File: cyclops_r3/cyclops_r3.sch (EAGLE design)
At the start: 102 parts, among them Q1 BC817, Q2 IRF510, U1 MCP4921, U2 MCP4022-50k, U3 317-N, U4 TLV3701, U5 337-N, U6 ADR03, U7 OP1177, U8 LTC2052HV, U9 ZXTD45

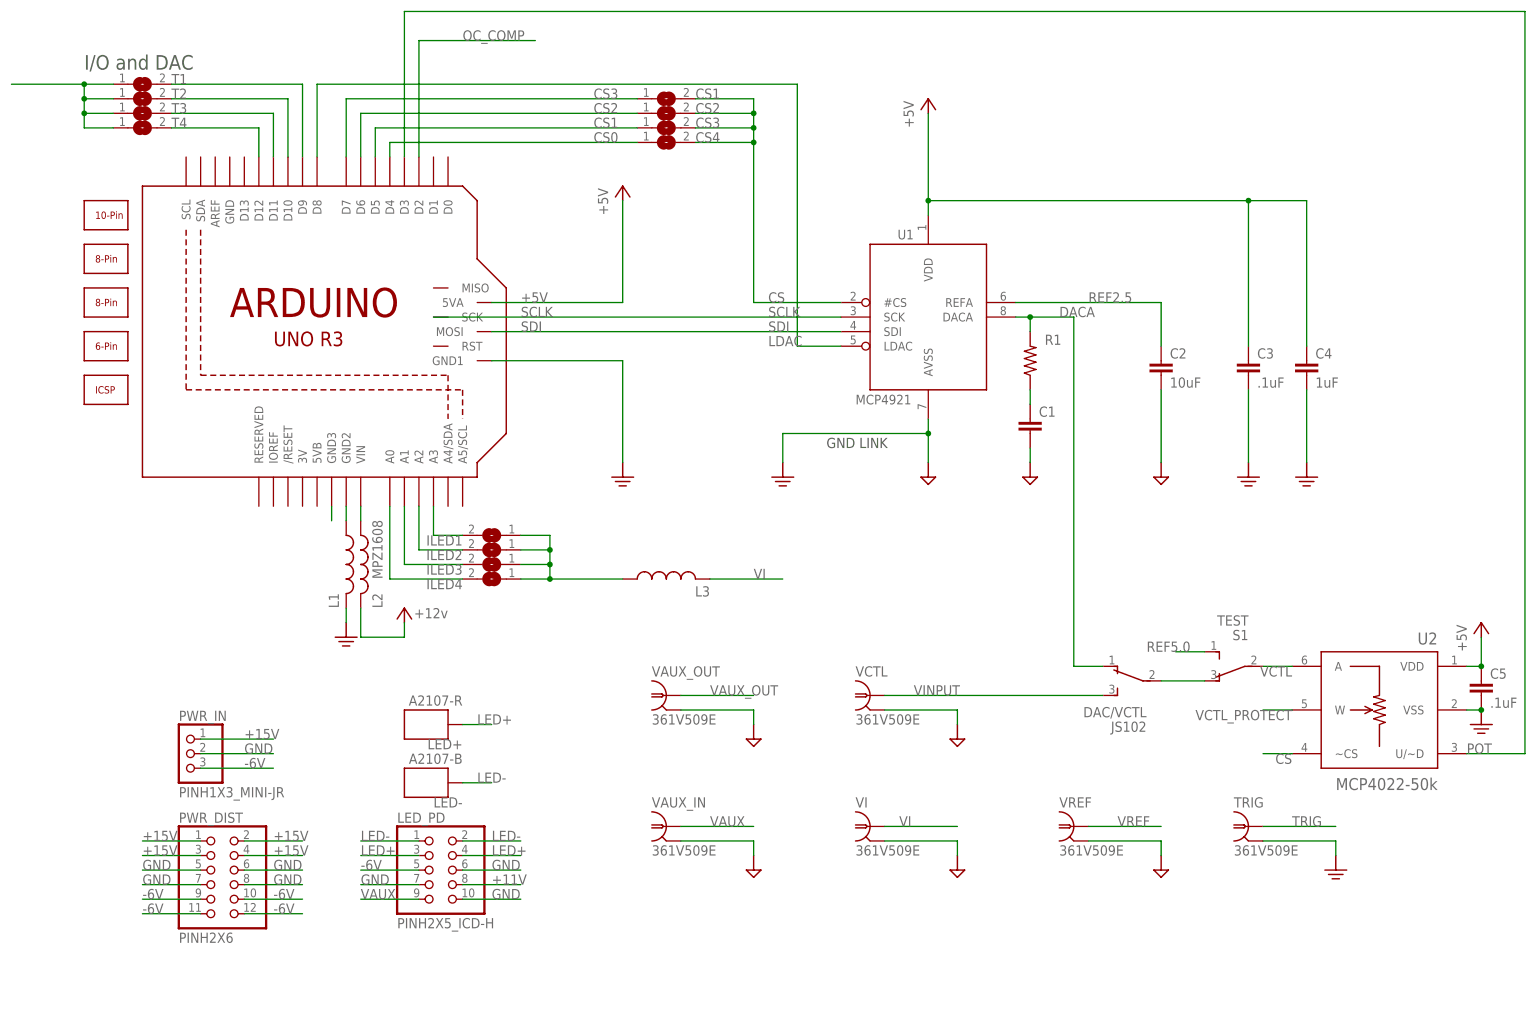
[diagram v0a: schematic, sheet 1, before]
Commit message: Added i2c line to the LED bus so that LEDs can come with eeprom.
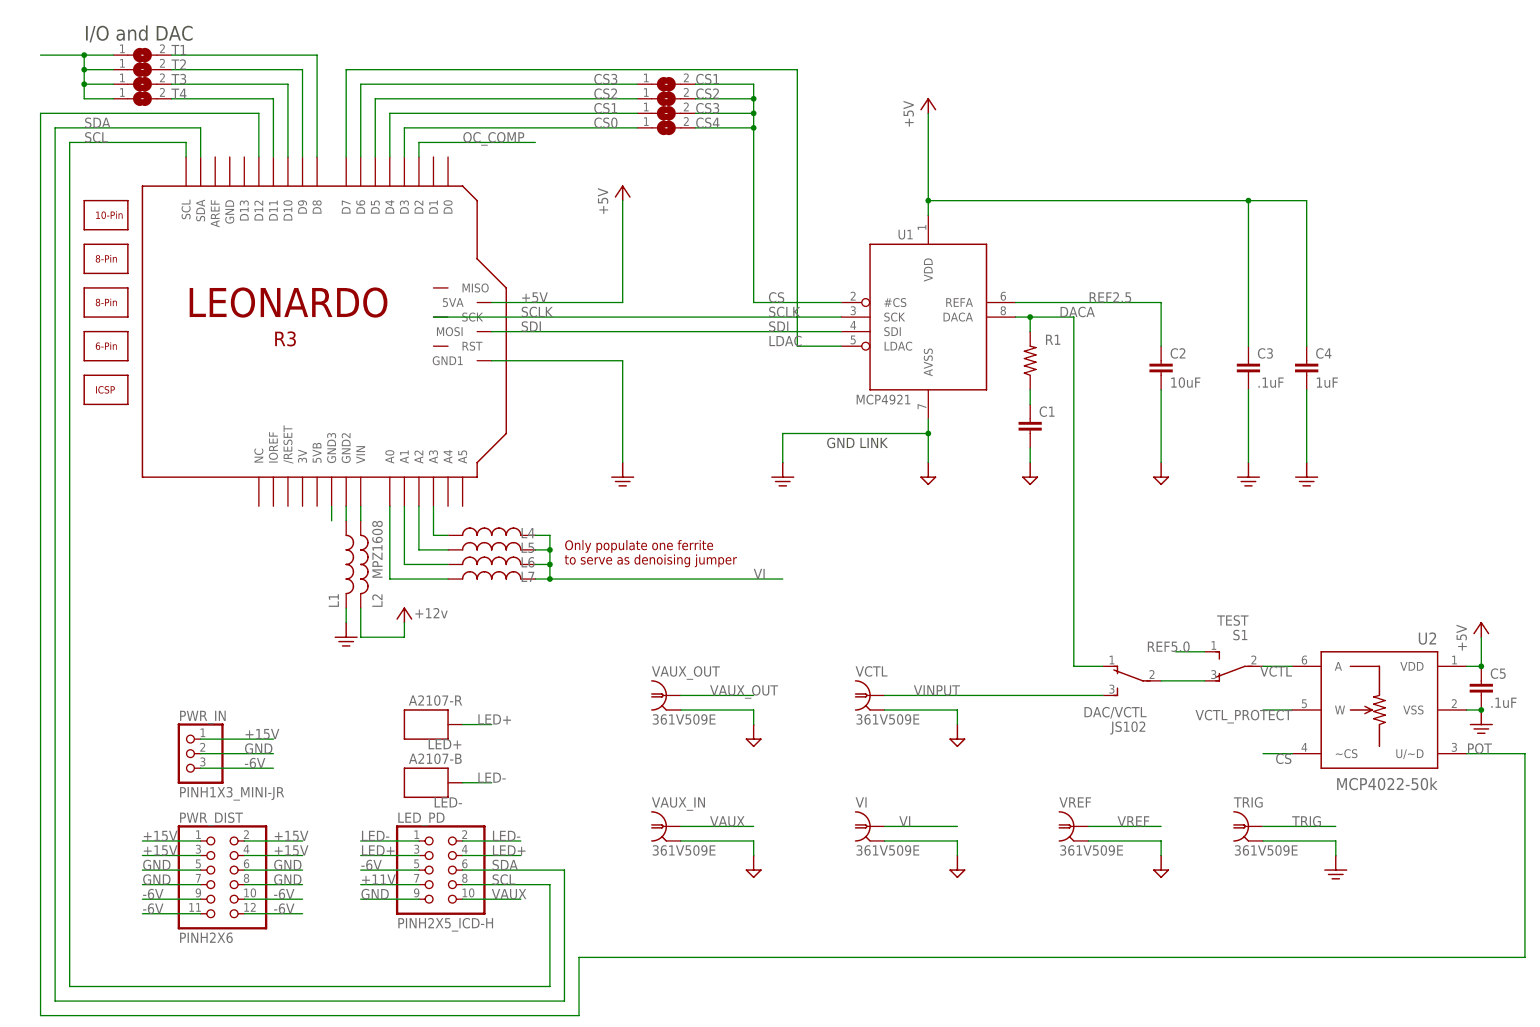
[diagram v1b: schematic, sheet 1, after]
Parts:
- removed ILED1, ILED2, ILED3, ILED4: (no value), cyclops:SJ
- removed L3: MPZ1608, cyclops:L_0603
- added L4, L5, L6, L7: MPZ1608, cyclops:L_0603
- LEONARDO: value ARDUINO_R3_ICSP_NOHOLES -> LEONARDO_R3_ICSP; device cyclops:ARDUINO_R3_ICSP_NOHOLES -> cyclops:LEONARDO_R3_ICSP
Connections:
- removed net N$56: ILED1.1, ILED2.1, ILED3.1, ILED4.1, L3.1
- new net SCL: LED_PD.8, LEONARDO.SCL
- new net SDA: LED_PD.6, LEONARDO.SDA
- net +11V: now also LED_PD.7; no longer LED_PD.8
- net CS0: now also LEONARDO.D3; no longer LEONARDO.D4
- net CS1: now also LEONARDO.D4; no longer LEONARDO.D5
- net CS2: now also LEONARDO.D5; no longer LEONARDO.D6
- net CS3: now also LEONARDO.D6; no longer LEONARDO.D7
- net GND: now also LED_PD.9; no longer LED_PD.10, LED_PD.6, LED_PD.7
- net LDAC: now also LEONARDO.D7; no longer LEONARDO.D8
- net N$19: now also L6.1
- net N$21: now also L5.1
- net N$23: now also L4.1
- net N$7: now also L7.1
- net POT: now also LEONARDO.D12; no longer LEONARDO.D3
- net T0: now also LEONARDO.D8; no longer LEONARDO.D9
- net T1: now also LEONARDO.D9; no longer LEONARDO.D10
- net T2: now also LEONARDO.D10; no longer LEONARDO.D11
- net T3: now also LEONARDO.D11; no longer LEONARDO.D12
- net VAUX: now also LED_PD.10; no longer LED_PD.9
- net VI: now also L4.2, L5.2, L6.2, L7.2; no longer L3.2
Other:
- note added: "MAX(VCTL) = 5.0V -- implies -- Max(VREF) ~ 0.75V Max(ILED) ~ 1.5 Amps"
- note added: "Only populate one ferrite to serve as denoising jumper"
- note removed: "MAX(VCTL) = 5.0V -- implies -- Max(VREF) ~ 1.5V Max(ILED) ~ 1.5 Amps"
- moved on the sheet: CS1, CS2, CS3, CS4, T1, T2, T3, T4

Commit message: Added arduino folder for creating the firmware for the board.
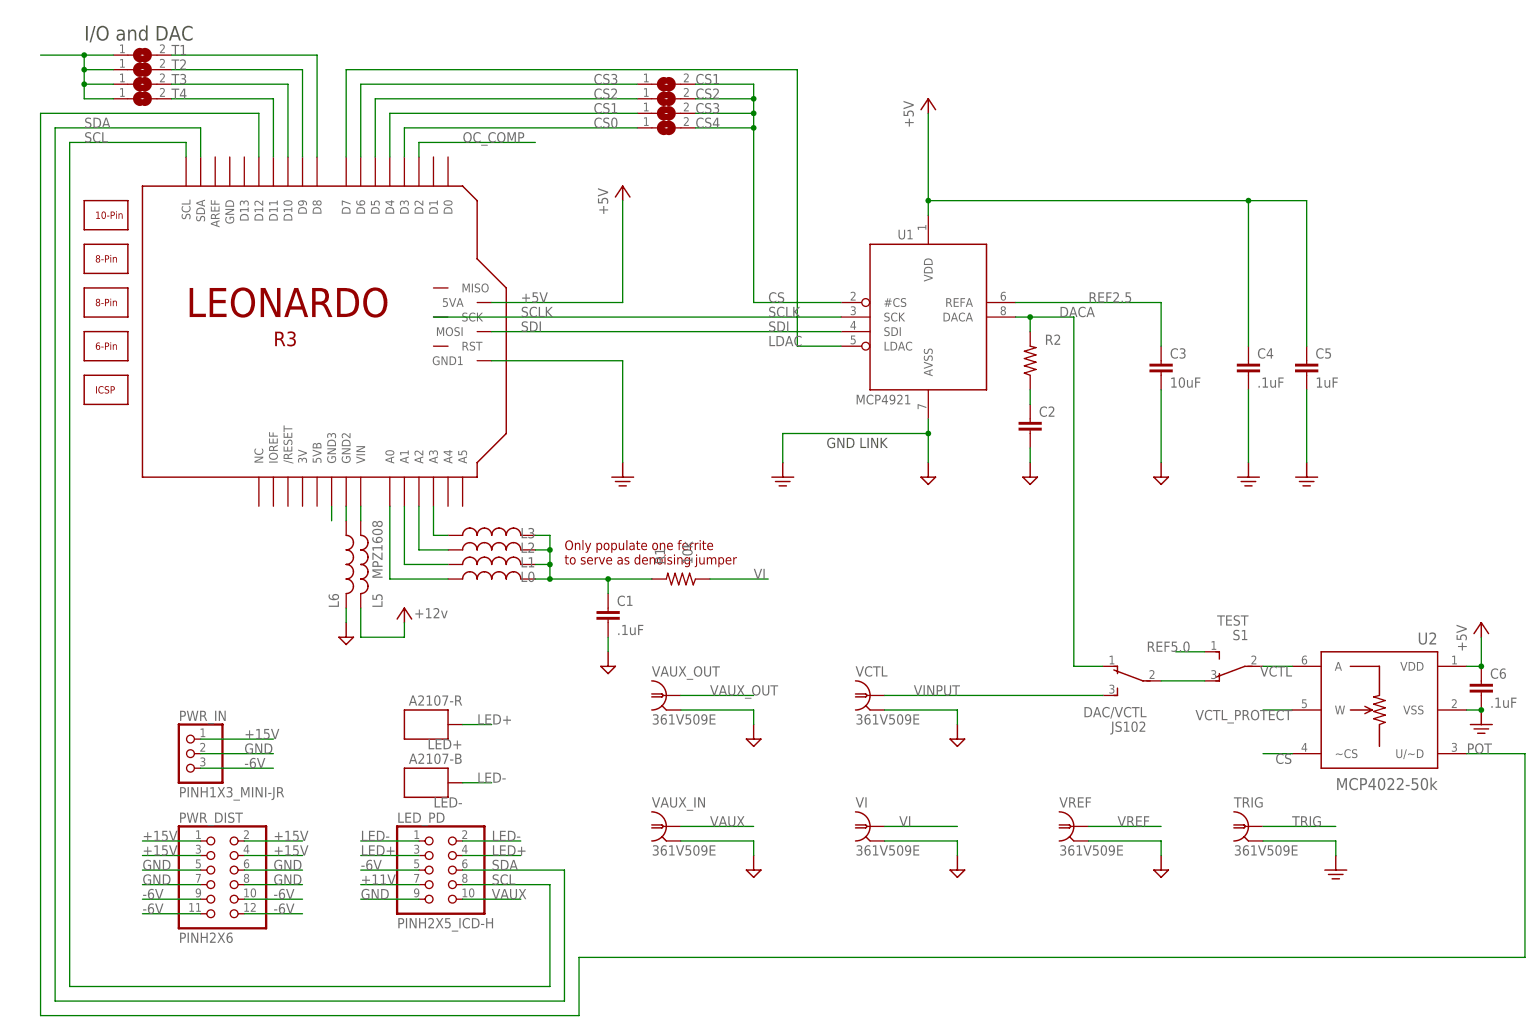
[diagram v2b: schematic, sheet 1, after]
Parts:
- added C24: 1uF, cyclops:C_0805
- added R25: 10, cyclops:R_0603
- C1: value (none) -> .1uF
- C10: value 100uF -> .1uF; device cyclops:C-POL_0807 -> cyclops:C_0603
- C12: value 1uF -> 100uF; device cyclops:C-POL_1206 -> cyclops:C-POL_0807
- C15: device cyclops:C_0805 -> cyclops:C-POL_1206
- C17, C5: value .1uF -> 1uF; device cyclops:C_0603 -> cyclops:C_0805
- C2: value 10uF -> (none); device cyclops:C_0805 -> cyclops:C_0603
- C22, C4: value 1uF -> .1uF; device cyclops:C_0805 -> cyclops:C_0603
- C3: value .1uF -> 10uF; device cyclops:C_0603 -> cyclops:C_0805
- C6: value 1uF -> .1uF; device cyclops:C-POL_1206 -> cyclops:C_0603
- C7: value .1uF -> 1uF; device cyclops:C_0603 -> cyclops:C-POL_1206
- C8: value 10uF -> .1uF; device cyclops:C-POL_1206 -> cyclops:C_0603
- C9: value .1uF -> 10uF; device cyclops:C_0603 -> cyclops:C-POL_1206
- R1: value (none) -> 10k
- R10: value 0 -> 1k
- R12: value 1k -> 0
- R13: value 470 -> 1k
- R15: value 1k -> 470
- R17: value 5.6k DNP -> 1k
- R18: value 220k -> 1k
- R19: value 1k -> 5.6k DNP
- R2: value 10k -> (none)
- R22: value 1k -> 220k
- R23: value 10 -> 1k
- R3: value 110k -> 10k
- R4: value 10k -> 110k
- R5: value 240 -> 10k
- R6: value 1.82k -> 240
- R7: value 10k -> 1.82k
- R8: value 3k -> 10k
- R9: value 1k -> 3k
- renumbered L4 to L3, L7 to L0
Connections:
- new net N$11: C1.1, L0.2, L1.2, L2.2, L3.2, R1.2
- net +11V: now also C10.1, C13.+, C19.1, C21.1, C23.1, L5.2, R10.2, R20.2, R4.1, R6.2; no longer C10.+, C15.1, C20.1, C22.1, C9.1, L2.2, R18.2, R3.1, R5.2, R8.2
- net +15V: now also C7.+; no longer C6.+
- net +5V: now also C6.1; no longer C3.1
- net -1.25V: now also C15.-, C22.1, C24.1, R22.1; no longer C14.-, C21.1, C23.1, R20.1
- net -6V: now also C14.-; no longer C13.-
- net COMP+: now also C8.1, R3.1; no longer C7.1, R2.1
- net DACA: now also R2.2; no longer R1.2
- net GND: now also C10.2, C13.-, C15.+, C24.2, C6.2, C7.-, C8.2, C9.-, L6.2, R12.2, R13.2, R16.1, R21.2, R24.2, R5.2, R7.1; no longer C10.-, C13.+, C15.2, C6.-, C7.2, C8.-, C9.2, L1.2, R10.2, R11.2, R14.1, R19.2, R22.2, R4.2, R6.1
- net KEEPOUT_GND: now also L6.1; no longer L1.1
- net N$1: now also C2.1, R2.1; no longer C1.1, R1.1
- net N$10: now also R25.1; no longer R23.1
- net N$12: now also R12.1; no longer R10.1
- net N$13: now also R25.2; no longer R23.2
- net N$14: now also L5.1; no longer L2.1
- net N$15: now also R23.1, R24.1; no longer R21.1, R22.1
- net N$16: now also R11.1; no longer R24.1
- net N$18: now also R13.1, R14.2; no longer R11.1, R12.2
- net N$19: now also L1.1; no longer L6.1
- net N$2: now also R10.1; no longer R9.1
- net N$20: now also R15.2; no longer R13.2
- net N$21: now also L2.1; no longer L5.1
- net N$22: now also R15.1; no longer R13.1
- net N$27: now also R8.2; no longer R7.2
- net N$28: now also R8.1; no longer R7.1
- net N$3: now also R9.1; no longer R8.1
- net N$5: now also R4.2, R5.1; no longer R3.2, R4.1
- net N$6: now also R16.2; no longer R14.2
- net N$72: now also C9.+, R6.1, R7.2; no longer C8.+, R5.1, R6.2
- net N$8: now also R18.1, R21.1; no longer R16.1, R19.1
- net OC_COMP: now also R11.2; no longer R24.2
- net REF2.5: now also C3.1; no longer C2.1
- net REF5.0: now also C20.1, R17.2; no longer C19.1, R15.2
- net VAUX: now also R20.1; no longer R18.1
- net VCTL: now also R19.2; no longer R17.2
- net VCTL_PROTECT: now also R19.1; no longer R17.1
- net VI: now also R1.1, R23.2, R3.2; no longer L0.2, L3.2, L5.2, L6.2, R2.2, R21.2
- net VREF: now also R18.2; no longer R16.2
- net VREFA2X1: now also R14.1, R17.1; no longer R12.1, R15.1
- net _VREF: now also R22.2; no longer R20.2
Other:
- moved on the sheet: C1, C10, C11, C12, C13, C14, C16, C17, C18, C19, C2, C21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

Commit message: Cleaned up BOM.
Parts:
- R19: value 5.6k DNP -> 5.6k(DNP)
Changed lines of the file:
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@@
 <part name="U$42" library="cyclops" deviceset="GND2" device=""/>
 <part name="U$43" library="cyclops" deviceset="GND2" device=""/>
-<part name="R19" library="cyclops" deviceset="R" device="_0603" value="5.6k DNP"/>
+<part name="R19" library="cyclops" deviceset="R" device="_0603" value="5.6k(DNP)"/>
 <part name="U$45" library="cyclops" deviceset="GND2" device=""/>
 <part name="P+4" library="cyclops" deviceset="+5V" device="" value="+12V"/>
@@
 <wire x1="93.98" y1="-30.48" x2="259.08" y2="-30.48" width="0.1524" layer="91"/>
 <wire x1="259.08" y1="-30.48" x2="259.08" y2="5.08" width="0.1524" layer="91"/>
-</segment>
-</net>
+<label x="7.62" y="116.84" size="1.778" layer="95"/>
+</segment>
+</net>

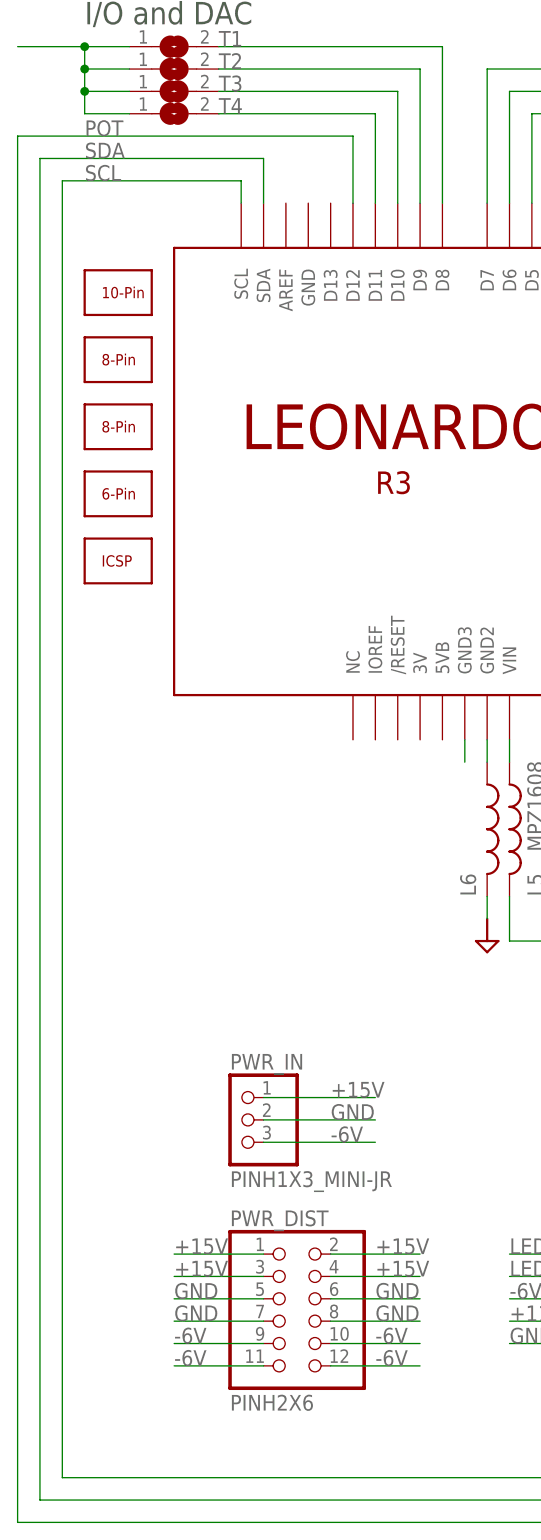
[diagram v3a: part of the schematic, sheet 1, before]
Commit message: Added pullups to the i2c bus to the PD interface.
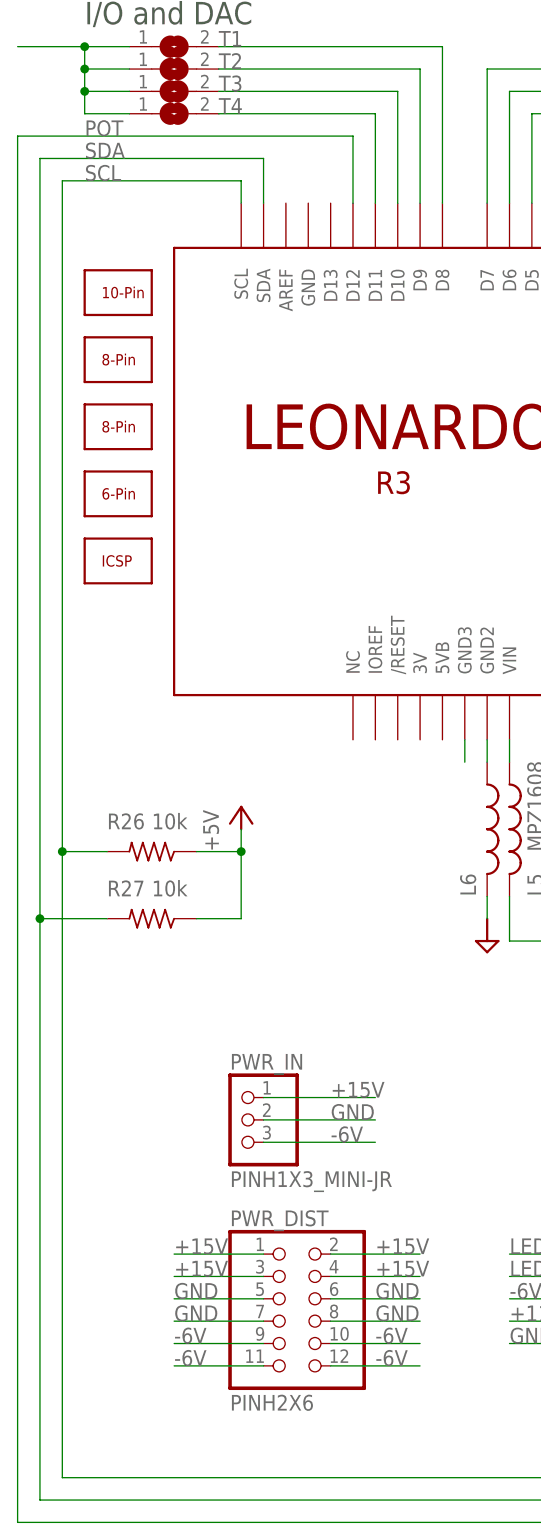
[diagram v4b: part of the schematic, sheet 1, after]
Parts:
- added R26, R27: 10k, cyclops:R_0603
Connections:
- net +5V: now also R26.1, R27.1
- net SCL: now also R26.2
- net SDA: now also R27.2
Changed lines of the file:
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@@
 <part name="U$50" library="cyclops" deviceset="GND2" device=""/>
 <part name="U$28" library="cyclops" deviceset="GND2" device=""/>
+<part name="R26" library="cyclops" deviceset="R" device="_0603" value="10k"/>
+<part name="R27" library="cyclops" deviceset="R" device="_0603" value="10k"/>
+<part name="P+7" library="cyclops" deviceset="+5V" device="" value="+5V"/>
 </parts>
 <sheets>
@@
 <instance part="U$50" gate="G$1" x="99.06" y="20.32"/>
 <instance part="U$28" gate="G$1" x="53.34" y="25.4"/>
+<instance part="R26" gate="R" x="15.24" y="35.56" smashed="yes" rot="R180">
+<attribute name="NAME" x="10.16" y="38.1" size="1.778" layer="95"/>
+<attribute name="VALUE" x="15.24" y="38.1" size="1.778" layer="96"/>
+</instance>
+<instance part="R27" gate="R" x="15.24" y="27.94" smashed="yes" rot="R180">
+<attribute name="NAME" x="10.16" y="30.48" size="1.778" layer="95"/>
+<attribute name="VALUE" x="15.24" y="30.48" size="1.778" layer="96"/>
+</instance>
+<instance part="P+7" gate="1" x="25.4" y="40.64"/>
 </instances>
 <busses>
@@
 <junction x="251.46" y="20.32"/>
 </segment>
+<segment>
+<pinref part="R27" gate="R" pin="1"/>
+<wire x1="20.32" y1="27.94" x2="25.4" y2="27.94" width="0.1524" layer="91"/>
+<wire x1="25.4" y1="27.94" x2="25.4" y2="35.56" width="0.1524" layer="91"/>
+<pinref part="R26" gate="R" pin="1"/>
+<wire x1="25.4" y1="35.56" x2="25.4" y2="38.1" width="0.1524" layer="91"/>
+<wire x1="20.32" y1="35.56" x2="25.4" y2="35.56" width="0.1524" layer="91"/>
+<junction x="25.4" y="35.56"/>
+</segment>
 </net>
 <net name="LED-" class="0">
@@
 <wire x1="27.94" y1="114.3" x2="2.54" y2="114.3" width="0.1524" layer="91"/>
 <label x="7.62" y="114.3" size="1.778" layer="95"/>
-<wire x1="2.54" y1="114.3" x2="2.54" y2="-38.1" width="0.1524" layer="91"/>
+<wire x1="2.54" y1="114.3" x2="2.54" y2="27.94" width="0.1524" layer="91"/>
+<wire x1="2.54" y1="27.94" x2="2.54" y2="-38.1" width="0.1524" layer="91"/>
 <wire x1="2.54" y1="-38.1" x2="91.44" y2="-38.1" width="0.1524" layer="91"/>
 <wire x1="91.44" y1="-38.1" x2="91.44" y2="-15.24" width="0.1524" layer="91"/>
@@
 <wire x1="73.66" y1="-15.24" x2="91.44" y2="-15.24" width="0.1524" layer="91"/>
 <label x="78.74" y="-15.24" size="1.778" layer="95"/>
+<pinref part="R27" gate="R" pin="2"/>
+<wire x1="2.54" y1="27.94" x2="10.16" y2="27.94" width="0.1524" layer="91"/>
+<junction x="2.54" y="27.94"/>
 </segment>
 </net>
@@
 <wire x1="25.4" y1="111.76" x2="5.08" y2="111.76" width="0.1524" layer="91"/>
 <label x="7.62" y="111.76" size="1.778" layer="95"/>
-<wire x1="5.08" y1="111.76" x2="5.08" y2="-35.56" width="0.1524" layer="91"/>
+<wire x1="5.08" y1="111.76" x2="5.08" y2="35.56" width="0.1524" layer="91"/>
+<wire x1="5.08" y1="35.56" x2="5.08" y2="-35.56" width="0.1524" layer="91"/>
 <wire x1="5.08" y1="-35.56" x2="88.9" y2="-35.56" width="0.1524" layer="91"/>
 <wire x1="88.9" y1="-35.56" x2="88.9" y2="-17.78" width="0.1524" layer="91"/>
@@
 <wire x1="73.66" y1="-17.78" x2="88.9" y2="-17.78" width="0.1524" layer="91"/>
 <label x="78.74" y="-17.78" size="1.778" layer="95"/>
-</segment>
-</net>
+<pinref part="R26" gate="R" pin="2"/>
+<wire x1="10.16" y1="35.56" x2="5.08" y2="35.56" width="0.1524" layer="91"/>
+<junction x="5.08" y="35.56"/>
+</segment>
+</net>
